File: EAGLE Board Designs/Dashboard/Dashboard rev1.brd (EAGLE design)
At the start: 67.9 x 27.6 mm, 46 parts, among them IC1 LM340S, J1 AVR-ISP-HEADER, U1 ATMEGA328P-AU, X1 CONNECTOR-6NANO-FIT_VERTICAL-6

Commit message: fixed a few traces
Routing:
- net RESET: track 24.4 -> 22.8 mm
- net N$19: track 38.8 -> 39.3 mm
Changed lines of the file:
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@@
 <rectangle x1="24.7523" y1="22.9235" x2="25.2095" y2="22.9997" layer="52" rot="R180"/>
 <rectangle x1="23.9903" y1="22.9235" x2="24.5999" y2="22.9997" layer="52" rot="R180"/>
-<rectangle x1="23.3045" y1="22.9235" x2="23.6855" y2="22.9997" layer="52" rot="R180"/>
+<rectangle x1="23.3045" y1="22.7711" x2="23.6855" y2="22.8473" layer="52" rot="R180"/>
 <rectangle x1="22.6187" y1="22.9235" x2="22.9997" y2="22.9997" layer="52" rot="R180"/>
 <rectangle x1="20.7899" y1="22.9235" x2="22.0091" y2="22.9997" layer="52" rot="R180"/>
@@
 <wire x1="10.2456" y1="19.5285" x2="10.2456" y2="20.0873" width="0.254" layer="1"/>
 <via x="10.2456" y="20.0873" extent="1-16" drill="0.35"/>
-<wire x1="10.2456" y1="20.0873" x2="13.5476" y2="23.3893" width="0.254" layer="16"/>
-<wire x1="13.5476" y1="23.3893" x2="42.7068" y2="23.3893" width="0.254" layer="16"/>
+<wire x1="10.2456" y1="20.0873" x2="13.9794" y2="23.8211" width="0.254" layer="16"/>
+<wire x1="42.275" y1="23.8211" x2="42.7068" y2="23.3893" width="0.254" layer="16"/>
+<wire x1="42.275" y1="23.8211" x2="13.9794" y2="23.8211" width="0.254" layer="16"/>
 <wire x1="15.5796" y1="23.1781" x2="15.5796" y2="21.6113" width="0.254" layer="1"/>
 <via x="15.5796" y="21.6113" extent="1-16" drill="0.35"/>
@@
 <wire x1="32.7246" y1="18.4109" x2="32.7246" y2="16.9123" width="0.508" layer="16"/>
 <wire x1="23.7076" y1="18.5633" x2="24.114" y2="18.9697" width="0.508" layer="16"/>
-<wire x1="29.5106" y1="7.7683" x2="27.7716" y2="7.7683" width="0.254" layer="1"/>
+<wire x1="29.5106" y1="7.7683" x2="28.1018" y2="7.7683" width="0.254" layer="1"/>
 <wire x1="21.9232" y1="20.7295" x2="21.9264" y2="20.7263" width="0.4064" layer="1"/>
 <wire x1="21.9264" y1="20.7263" x2="22.4344" y2="20.7263" width="0.4064" layer="1"/>
@@
 <wire x1="22.8694" y1="4.3487625" x2="20.3802" y2="6.8379625" width="0.254" layer="1"/>
 <wire x1="20.3802" y1="19.4428375" x2="20.3802" y2="6.8379625" width="0.254" layer="1"/>
-<wire x1="27.7716" y1="7.7683" x2="27.0096" y2="7.0063" width="0.254" layer="1"/>
-<wire x1="27.0096" y1="3.8821" x2="26.146" y2="3.0185" width="0.254" layer="1"/>
+<wire x1="28.1018" y1="7.7683" x2="27.5938" y2="7.2603" width="0.254" layer="1"/>
+<wire x1="27.5938" y1="4.4663" x2="26.146" y2="3.0185" width="0.254" layer="1"/>
 <wire x1="26.146" y1="3.0185" x2="24.2156" y2="3.0185" width="0.254" layer="1"/>
 <wire x1="24.2156" y1="3.0185" x2="22.9202" y2="4.3139" width="0.254" layer="1"/>
 <wire x1="22.9202" y1="4.3139" x2="22.8694" y2="4.3139" width="0.254" layer="1"/>
-<wire x1="27.0096" y1="7.0063" x2="27.0096" y2="3.8821" width="0.254" layer="1"/>
+<wire x1="27.5938" y1="7.2603" x2="27.5938" y2="4.4663" width="0.254" layer="1"/>
 <wire x1="28.6996" y1="4.3393" x2="27.3788" y2="3.0185" width="0.254" layer="1"/>
 <wire x1="27.3788" y1="3.0185" x2="26.146" y2="3.0185" width="0.254" layer="1"/>
@@
 <wire x1="35.99806875" y1="13.8325" x2="36.7198" y2="13.8325" width="0.254" layer="1"/>
 <contactref element="J1" pad="5"/>
-<wire x1="35.1376" y1="12.7213" x2="31.8102" y2="9.3939" width="0.254" layer="16"/>
-<wire x1="31.8102" y1="9.3939" x2="25.4094" y2="9.3939" width="0.254" layer="16"/>
-<wire x1="35.1376" y1="12.7213" x2="35.163" y2="12.6959" width="0.254" layer="16"/>
-<wire x1="35.163" y1="12.6959" x2="35.163" y2="7.9207" width="0.254" layer="16"/>
-<wire x1="31.5816" y1="4.3393" x2="35.163" y2="7.9207" width="0.254" layer="16"/>
 <via x="31.5816" y="4.3393" extent="1-16" drill="0.35"/>
 <wire x1="31.5816" y1="4.3393" x2="30.3996" y2="4.3393" width="0.254" layer="1"/>
+<wire x1="35.1376" y1="12.7213" x2="28.7368" y2="12.7213" width="0.254" layer="16"/>
+<wire x1="28.7368" y1="12.7213" x2="25.4094" y2="9.3939" width="0.254" layer="16"/>
+<wire x1="25.4094" y1="9.3939" x2="25.6888" y2="9.1145" width="0.254" layer="16"/>
+<wire x1="25.6634" y1="9.1145" x2="25.6888" y2="9.1145" width="0.254" layer="16"/>
+<wire x1="30.4386" y1="4.3393" x2="25.6634" y2="9.1145" width="0.254" layer="16"/>
+<wire x1="30.4386" y1="4.3393" x2="31.5816" y2="4.3393" width="0.254" layer="16"/>
 </signal>
 <signal name="+12V">
@@
 <wire x1="11.8585" y1="19.03463125" x2="11.8585" y2="16.9504" width="0.254" layer="16"/>
 <wire x1="44.5765875" y1="20.0873" x2="44.6118" y2="20.0873" width="0.254" layer="16"/>
-<wire x1="42.3949875" y1="22.2689" x2="44.5765875" y2="20.0873" width="0.254" layer="16"/>
-<wire x1="11.8585" y1="19.03463125" x2="15.09276875" y2="22.2689" width="0.254" layer="16"/>
-<wire x1="15.09276875" y1="22.2689" x2="42.3949875" y2="22.2689" width="0.254" layer="16"/>
+<wire x1="41.7599875" y1="22.9039" x2="44.5765875" y2="20.0873" width="0.254" layer="16"/>
+<wire x1="11.8585" y1="19.03463125" x2="15.72776875" y2="22.9039" width="0.254" layer="16"/>
+<wire x1="15.72776875" y1="22.9039" x2="41.7599875" y2="22.9039" width="0.254" layer="16"/>
 </signal>
 <signal name="N$8">

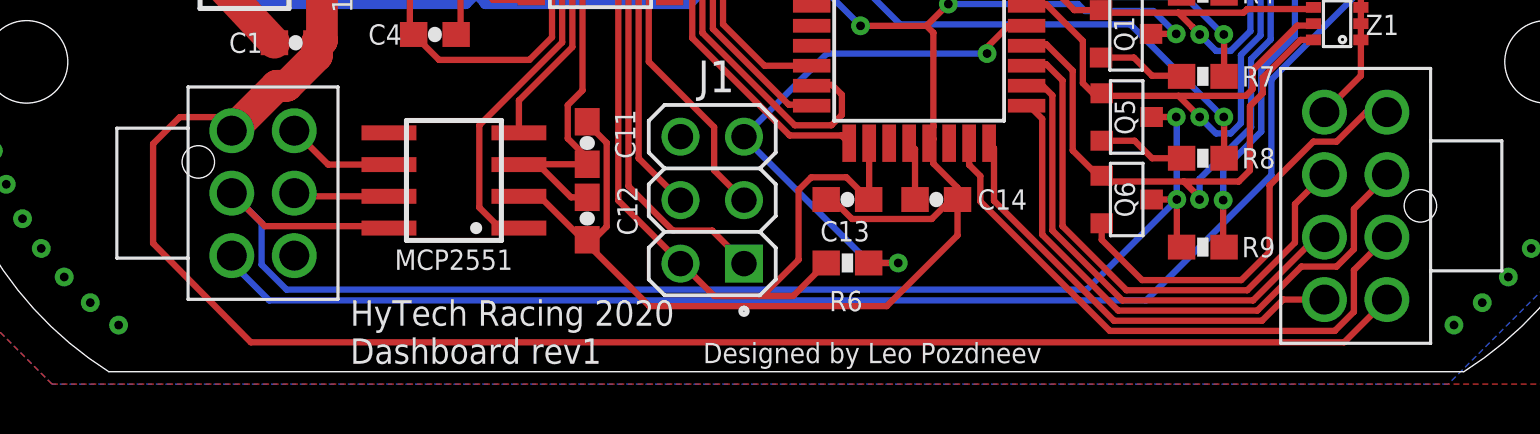
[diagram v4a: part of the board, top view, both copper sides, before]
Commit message: added a zener to regulate voltage on the buzzer
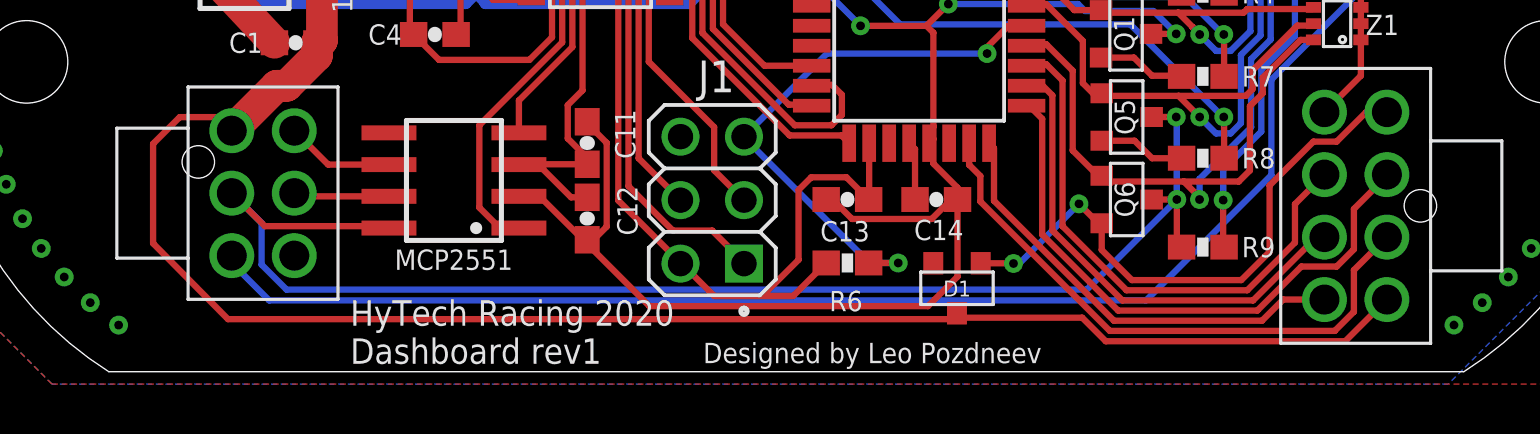
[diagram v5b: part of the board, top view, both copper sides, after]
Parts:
- added D1: DIODE_ZENER, HyTechDevices:SOT23
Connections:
- net +12V: now also D1.3
- net BUZZER_OUT: now also D1.1
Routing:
- net BUZZER_OUT: track 17.1 -> 23.5 mm, vias 0 -> 2
- net GND: track 294.8 -> 295.7 mm
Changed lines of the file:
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@@
 </element>
 <element name="C14" library="HyTechDevices" package="0603-CAP" value=".1uF" x="33.1056" y="6.8793" smashed="yes">
-<attribute name="NAME" x="34.7566" y="6.4729" size="0.8128" layer="25" font="vector"/>
+<attribute name="NAME" x="32.2166" y="5.2537" size="0.8128" layer="25" font="vector"/>
 </element>
 <element name="C13" library="HyTechDevices" package="0603-CAP" value="0.1uF" x="29.5496" y="6.8793" smashed="yes" rot="R180">
@@
 <attribute name="NAME" x="25.0284" y="12.4419" size="1.27" layer="25" font="vector" rot="R180"/>
 <attribute name="VALUE" x="28.5844" y="3.0439" size="1.27" layer="27" font="vector" rot="R90"/>
+</element>
+<element name="D1" library="HyTechDevices" package="SOT23" value="DIODE_ZENER" x="33.9344" y="3.3274" smashed="yes" rot="R180">
+<attribute name="NAME" x="33.9344" y="2.9972" size="0.635" layer="25" rot="R180" align="top-center"/>
+<attribute name="VALUE" x="32.5374" y="2.4384" size="0.3048" layer="27" rot="R180" align="bottom-center"/>
 </element>
 </elements>
@@
 <wire x1="32.92133125" y1="6.0999" x2="33.70073125" y2="6.8793" width="0.254" layer="1"/>
 <wire x1="29.73386875" y1="6.0999" x2="32.92133125" y2="6.0999" width="0.254" layer="1"/>
-<wire x1="33.9556" y1="6.8793" x2="33.9556" y2="5.4433" width="0.254" layer="1"/>
-<wire x1="31.1244" y1="2.6121" x2="21.6248" y2="2.6121" width="0.254" layer="1"/>
+<wire x1="33.9556" y1="6.8793" x2="33.9556" y2="3.7923" width="0.254" layer="1"/>
+<wire x1="32.7754" y1="2.6121" x2="21.6248" y2="2.6121" width="0.254" layer="1"/>
 <wire x1="21.6248" y1="2.6121" x2="19.0526" y2="5.1843" width="0.254" layer="1"/>
-<wire x1="33.9556" y1="5.4433" x2="31.1244" y2="2.6121" width="0.254" layer="1"/>
+<wire x1="33.9556" y1="3.7923" x2="32.7754" y2="2.6121" width="0.254" layer="1"/>
 <wire x1="50.0982" y1="13.2674" x2="50.0982" y2="11.8339" width="0.254" layer="1"/>
 <wire x1="50.0982" y1="11.8339" x2="48.6396" y2="10.3753" width="0.254" layer="1"/>
@@
 <wire x1="8.3176" y1="13.1531" x2="8.5184" y2="13.2411" width="1.27" layer="1"/>
 <wire x1="8.5184" y1="15.4899" x2="8.5184" y2="13.2411" width="1.27" layer="1"/>
-<wire x1="51.1396" y1="2.8753" x2="49.4286" y2="1.1643" width="0.254" layer="1"/>
 <wire x1="1.762" y1="9.1093875" x2="1.762" y2="5.124375" width="0.254" layer="1"/>
 <wire x1="1.762" y1="9.1093875" x2="2.8289125" y2="10.1763" width="0.254" layer="1"/>
@@
 <wire x1="7.112" y1="11.43" x2="8.3176" y2="12.6356" width="1.27" layer="1"/>
 <wire x1="8.3176" y1="12.6356" x2="8.3176" y2="13.1531" width="1.27" layer="1"/>
-<wire x1="1.762" y1="5.124375" x2="5.673853125" y2="1.1643" width="0.254" layer="1"/>
-<wire x1="5.673853125" y1="1.1643" x2="49.4286" y2="1.1643" width="0.254" layer="1"/>
+<wire x1="1.762" y1="5.124375" x2="4.758734375" y2="2.0907" width="0.254" layer="1"/>
+<contactref element="D1" pad="3"/>
+<wire x1="38.94521875" y1="2.1496" x2="34.1122" y2="2.1496" width="0.254" layer="1"/>
+<wire x1="34.1122" y1="2.1496" x2="33.9344" y2="2.3274" width="0.254" layer="1"/>
+<wire x1="51.1396" y1="2.8753" x2="49.4713" y2="1.207" width="0.254" layer="1"/>
+<wire x1="49.4713" y1="1.207" x2="39.88781875" y2="1.207" width="0.254" layer="1"/>
+<wire x1="39.88781875" y1="1.207" x2="38.94521875" y2="2.1496" width="0.254" layer="1"/>
+<wire x1="33.9344" y1="2.3274" x2="33.6977" y2="2.0907" width="0.254" layer="1"/>
+<wire x1="33.6977" y1="2.0907" x2="4.758734375" y2="2.0907" width="0.254" layer="1"/>
 </signal>
 <signal name="BUZZER_CTRL">
@@
 <signal name="BUZZER_OUT">
 <contactref element="Q6" pad="2"/>
-<wire x1="39.7256" y1="5.9293" x2="39.7256" y2="5.2689" width="0.254" layer="1"/>
-<wire x1="41.341" y1="3.6535" x2="39.7256" y2="5.2689" width="0.254" layer="1"/>
-<wire x1="41.341" y1="3.6535" x2="45.31173125" y2="3.6535" width="0.254" layer="1"/>
+<wire x1="39.7256" y1="5.9293" x2="39.7256" y2="4.8625" width="0.254" layer="1"/>
+<wire x1="40.9346" y1="3.6535" x2="39.7256" y2="4.8625" width="0.254" layer="1"/>
+<wire x1="40.9346" y1="3.6535" x2="45.31173125" y2="3.6535" width="0.254" layer="1"/>
 <wire x1="45.31173125" y1="3.6535" x2="46.4442" y2="4.78596875" width="0.254" layer="1"/>
 <contactref element="$$X2" pad="P$4"/>
@@
 <wire x1="46.4442" y1="4.78596875" x2="46.4442" y2="7.4425" width="0.254" layer="1"/>
 <wire x1="46.4442" y1="7.4425" x2="48.1976" y2="9.1959" width="0.254" layer="1"/>
+<contactref element="D1" pad="1"/>
+<wire x1="36.195" y1="4.318" x2="36.1856" y2="4.3274" width="0.254" layer="1"/>
+<wire x1="36.1856" y1="4.3274" x2="34.8844" y2="4.3274" width="0.254" layer="1"/>
+<via x="36.195" y="4.318" extent="1-16" drill="0.35"/>
+<wire x1="36.195" y1="4.318" x2="36.428" y2="4.318" width="0.254" layer="16"/>
+<wire x1="36.428" y1="4.318" x2="38.8156" y2="6.7056" width="0.254" layer="16"/>
+<via x="38.8156" y="6.7056" extent="1-16" drill="0.35"/>
+<wire x1="38.8156" y1="6.7056" x2="39.5919" y2="5.9293" width="0.254" layer="1"/>
+<wire x1="39.5919" y1="5.9293" x2="39.7256" y2="5.9293" width="0.254" layer="1"/>
 </signal>
 <signal name="N$4">

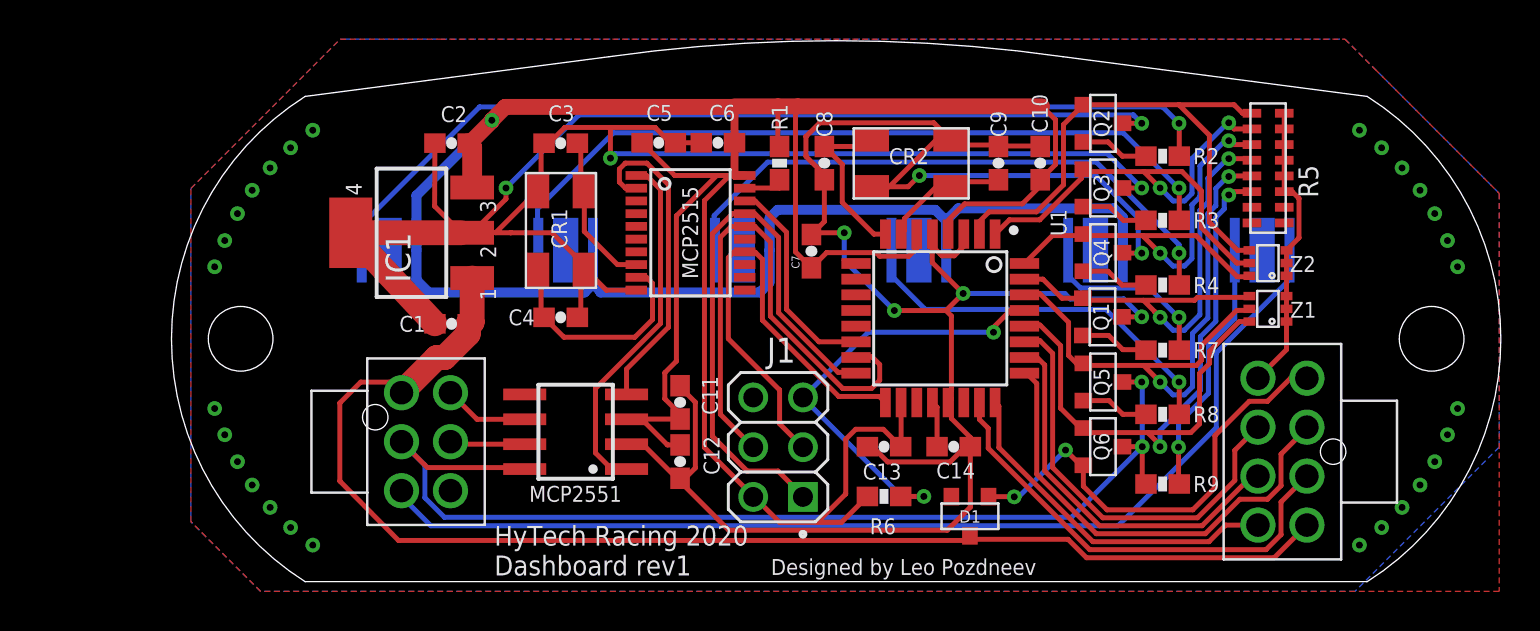
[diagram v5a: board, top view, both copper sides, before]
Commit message: added via stiching around the board
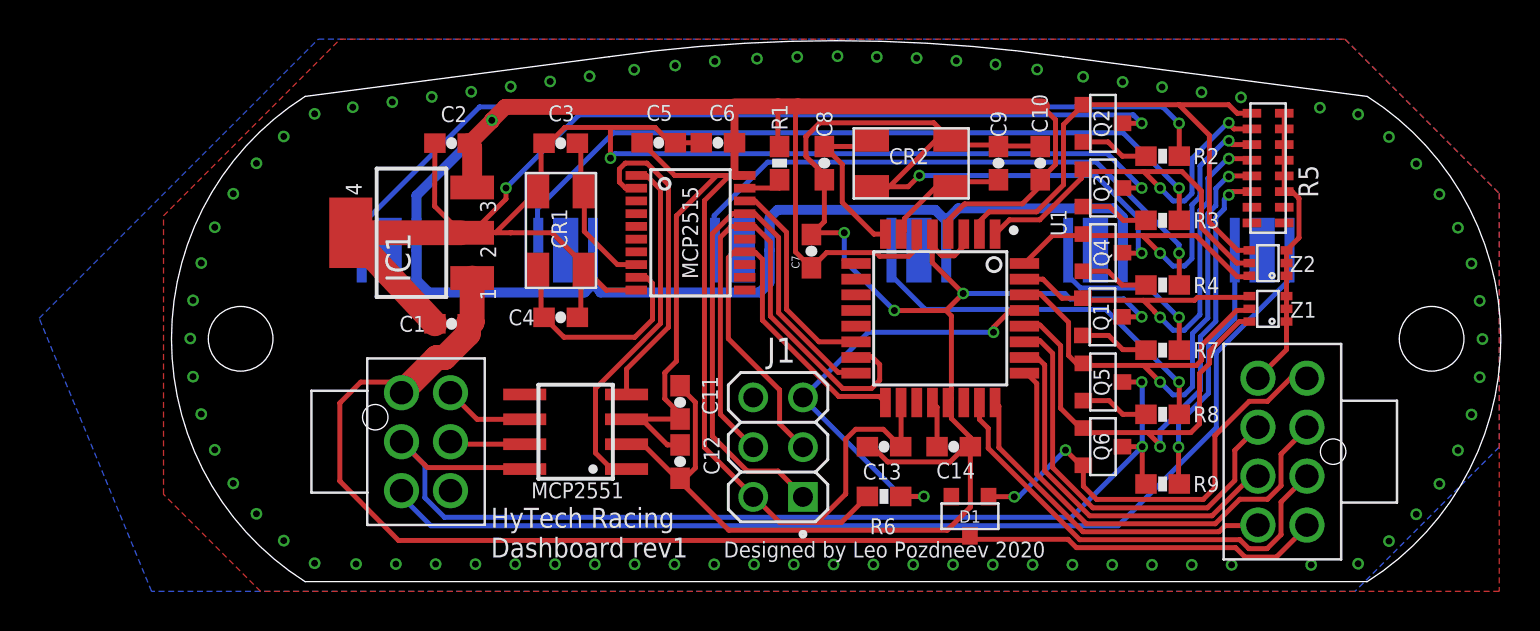
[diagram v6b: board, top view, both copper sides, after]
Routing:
- net GND: vias 40 -> 79
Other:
- board text added: "Designed by Leo Pozdneev 2020"
- board text added: "HyTech Racing Dashboard rev1"
- board text removed: "Designed by Leo Pozdneev"
- board text removed: "HyTech Racing 2020 Dashboard rev1"
